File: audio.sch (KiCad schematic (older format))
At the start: 25 parts, among them U6 UDA1334A, U7 LM386, U8 LM386

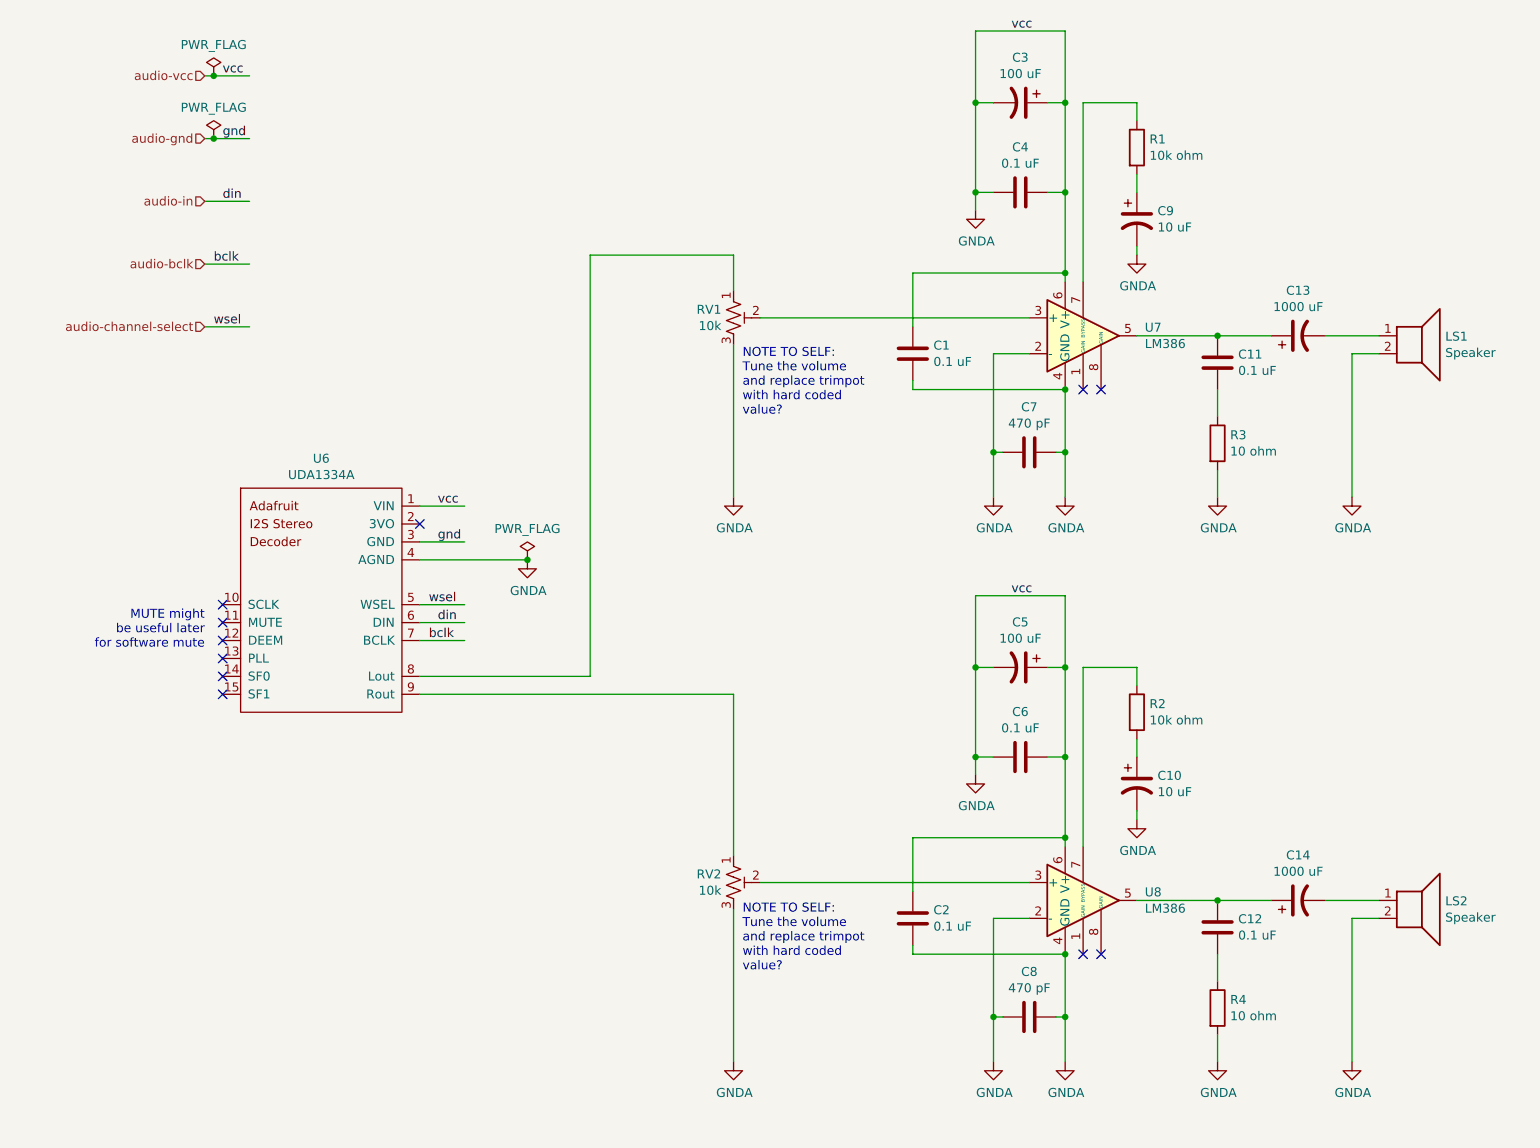
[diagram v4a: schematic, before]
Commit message: Reassign schematic annotation
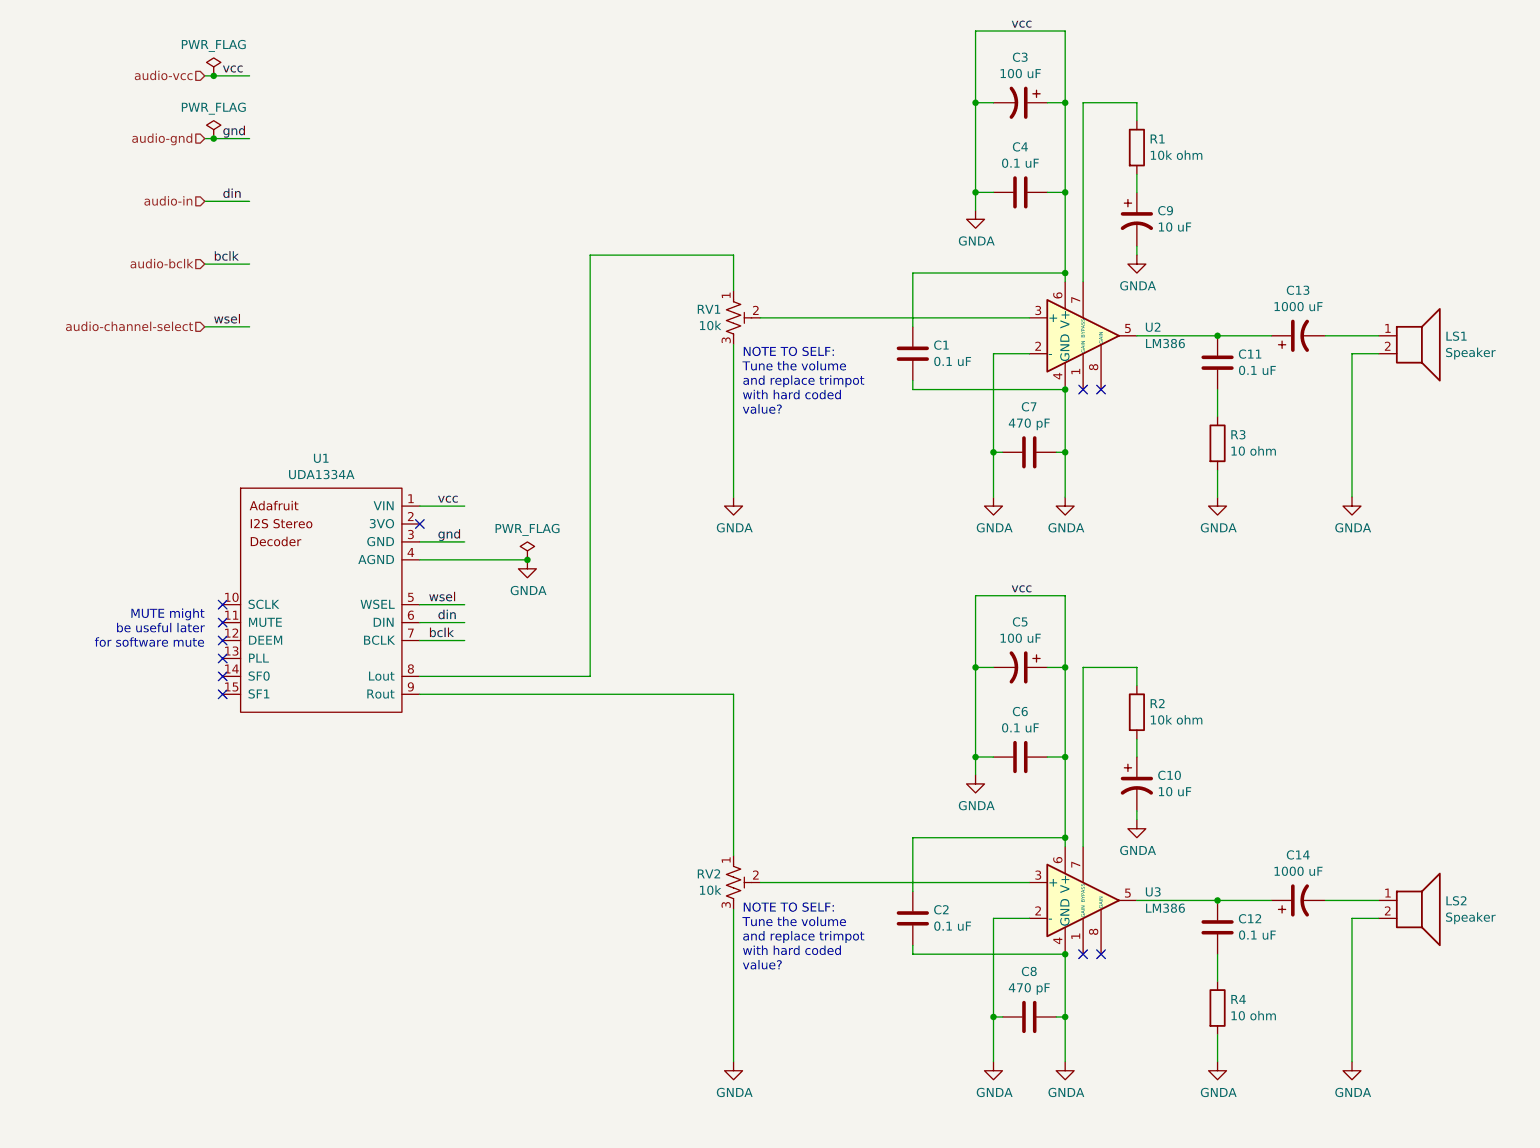
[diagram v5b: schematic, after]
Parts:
- renumbered U6 to U1, U7 to U2, U8 to U3
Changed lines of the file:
@@
 $EndDescr
 $Comp
-L Amplifier_Audio:LM386 U7
+L Amplifier_Audio:LM386 U2
 U 1 1 60687AB3
 P 6600 2350
-F 0 "U7" H 6944 2396 50  0000 L CNN
+F 0 "U2" H 6944 2396 50  0000 L CNN
 F 1 "LM386" H 6944 2305 50  0000 L CNN
 F 2 "" H 6700 2450 50  0001 C CNN
@@
 	4800 2250 6300 2250
 $Comp
-L Amplifier_Audio:LM386 U8
+L Amplifier_Audio:LM386 U3
 U 1 1 606DD65F
 P 6600 5500
-F 0 "U8" H 6944 5546 50  0000 L CNN
+F 0 "U3" H 6944 5546 50  0000 L CNN
 F 1 "LM386" H 6944 5455 50  0000 L CNN
 F 2 "" H 6700 5600 50  0001 C CNN
@@
 	4800 5400 6300 5400
 $Comp
-L adafruit:UDA1334A U6
+L adafruit:UDA1334A U1
 U 1 1 6067F8B5
 P 2350 3850
-F 0 "U6" H 2350 4665 50  0000 C CNN
+F 0 "U1" H 2350 4665 50  0000 C CNN
 F 1 "UDA1334A" H 2350 4574 50  0000 C CNN
 F 2 "" H 2150 4550 50  0001 C CNN
@@
 	2900 3850 3150 3850
 $Comp
-L power:PWR_FLAG #FLG0102
+L power:PWR_FLAG #FLG02
 U 1 1 606CA04F
 P 1750 1250
-F 0 "#FLG0102" H 1750 1325 50  0001 C CNN
+F 0 "#FLG02" H 1750 1325 50  0001 C CNN
 F 1 "PWR_FLAG" H 1750 1423 50  0000 C CNN
 F 2 "" H 1750 1250 50  0001 C CNN
@@
 	1700 900  1750 900
 $Comp
-L power:PWR_FLAG #FLG0101
+L power:PWR_FLAG #FLG01
 U 1 1 6070660E
 P 1750 900
-F 0 "#FLG0101" H 1750 975 50  0001 C CNN
+F 0 "#FLG01" H 1750 975 50  0001 C CNN
 F 1 "PWR_FLAG" H 1750 1073 50  0000 C CNN
 F 2 "" H 1750 900 50  0001 C CNN
@@
 	1750 900  1950 900
 $Comp
-L power:GNDA #PWR0103
+L power:GNDA #PWR08
 U 1 1 6070E011
 P 6100 3250
-F 0 "#PWR0103" H 6100 3000 50  0001 C CNN
+F 0 "#PWR08" H 6100 3000 50  0001 C CNN
 F 1 "GNDA" H 6105 3077 50  0000 C CNN
 F 2 "" H 6100 3250 50  0001 C CNN
@@
 $EndComp
 $Comp
-L power:GNDA #PWR0104
+L power:GNDA #PWR010
 U 1 1 6070E631
 P 6500 3250
-F 0 "#PWR0104" H 6500 3000 50  0001 C CNN
+F 0 "#PWR010" H 6500 3000 50  0001 C CNN
 F 1 "GNDA" H 6505 3077 50  0000 C CNN
 F 2 "" H 6500 3250 50  0001 C CNN
@@
 $EndComp
 $Comp
-L power:GNDA #PWR0105
+L power:GNDA #PWR014
 U 1 1 6070EF51
 P 7350 3250
-F 0 "#PWR0105" H 7350 3000 50  0001 C CNN
+F 0 "#PWR014" H 7350 3000 50  0001 C CNN
 F 1 "GNDA" H 7355 3077 50  0000 C CNN
 F 2 "" H 7350 3250 50  0001 C CNN
@@
 $EndComp
 $Comp
-L power:GNDA #PWR0106
+L power:GNDA #PWR016
 U 1 1 6070F2C0
 P 8100 3250
-F 0 "#PWR0106" H 8100 3000 50  0001 C CNN
+F 0 "#PWR016" H 8100 3000 50  0001 C CNN
 F 1 "GNDA" H 8105 3077 50  0000 C CNN
 F 2 "" H 8100 3250 50  0001 C CNN
@@
 $EndComp
 $Comp
-L power:GNDA #PWR0107
+L power:GNDA #PWR04
 U 1 1 6070F50A
 P 4650 3250
-F 0 "#PWR0107" H 4650 3000 50  0001 C CNN
+F 0 "#PWR04" H 4650 3000 50  0001 C CNN
 F 1 "GNDA" H 4655 3077 50  0000 C CNN
 F 2 "" H 4650 3250 50  0001 C CNN
@@
 $EndComp
 $Comp
-L power:GNDA #PWR0108
+L power:GNDA #PWR09
 U 1 1 60711E7C
 P 6100 6400
-F 0 "#PWR0108" H 6100 6150 50  0001 C CNN
+F 0 "#PWR09" H 6100 6150 50  0001 C CNN
 F 1 "GNDA" H 6105 6227 50  0000 C CNN
 F 2 "" H 6100 6400 50  0001 C CNN
@@
 $EndComp
 $Comp
-L power:GNDA #PWR0109
+L power:GNDA #PWR011
 U 1 1 60711E82
 P 6500 6400
-F 0 "#PWR0109" H 6500 6150 50  0001 C CNN
+F 0 "#PWR011" H 6500 6150 50  0001 C CNN
 F 1 "GNDA" H 6505 6227 50  0000 C CNN
 F 2 "" H 6500 6400 50  0001 C CNN
@@
 $EndComp
 $Comp
-L power:GNDA #PWR0110
+L power:GNDA #PWR015
 U 1 1 60711E88
 P 7350 6400
-F 0 "#PWR0110" H 7350 6150 50  0001 C CNN
+F 0 "#PWR015" H 7350 6150 50  0001 C CNN
 F 1 "GNDA" H 7355 6227 50  0000 C CNN
 F 2 "" H 7350 6400 50  0001 C CNN
@@
 $EndComp
 $Comp
-L power:GNDA #PWR0111
+L power:GNDA #PWR017
 U 1 1 60711E8E
 P 8100 6400
-F 0 "#PWR0111" H 8100 6150 50  0001 C CNN
+F 0 "#PWR017" H 8100 6150 50  0001 C CNN
 F 1 "GNDA" H 8105 6227 50  0000 C CNN
 F 2 "" H 8100 6400 50  0001 C CNN
@@
 $EndComp
 $Comp
-L power:GNDA #PWR0112
+L power:GNDA #PWR05
 U 1 1 60711E94
 P 4650 6400
-F 0 "#PWR0112" H 4650 6150 50  0001 C CNN
+F 0 "#PWR05" H 4650 6150 50  0001 C CNN
 F 1 "GNDA" H 4655 6227 50  0000 C CNN
 F 2 "" H 4650 6400 50  0001 C CNN
@@
 Connection ~ 3500 3600
 $Comp
-L power:PWR_FLAG #FLG0105
+L power:PWR_FLAG #FLG03
 U 1 1 60765574
 P 3500 3600
-F 0 "#FLG0105" H 3500 3675 50  0001 C CNN
+F 0 "#FLG03" H 3500 3675 50  0001 C CNN
 F 1 "PWR_FLAG" H 3500 3773 50  0000 C CNN
 F 2 "" H 3500 3600 50  0001 C CNN
@@
 $EndComp
 $Comp
-L power:GNDA #PWR0113
+L power:GNDA #PWR03
 U 1 1 607206A1
 P 3500 3600
-F 0 "#PWR0113" H 3500 3350 50  0001 C CNN
+F 0 "#PWR03" H 3500 3350 50  0001 C CNN
 F 1 "GNDA" H 3505 3427 50  0000 C CNN
 F 2 "" H 3500 3600 50  0001 C CNN
@@
 	2900 3600 3500 3600
 $Comp
-L power:GNDA #PWR?
+L power:GNDA #PWR012
 U 1 1 60779F44
 P 6900 1900
-F 0 "#PWR?" H 6900 1650 50  0001 C CNN
+F 0 "#PWR012" H 6900 1650 50  0001 C CNN
 F 1 "GNDA" H 6905 1727 50  0000 C CNN
 F 2 "" H 6900 1900 50  0001 C CNN
@@
 $EndComp
 $Comp
-L power:GNDA #PWR?
+L power:GNDA #PWR06
 U 1 1 6077CCCE
 P 6000 1650
-F 0 "#PWR?" H 6000 1400 50  0001 C CNN
+F 0 "#PWR06" H 6000 1400 50  0001 C CNN
 F 1 "GNDA" H 6005 1477 50  0000 C CNN
 F 2 "" H 6000 1650 50  0001 C CNN
@@
 $EndComp
 $Comp
-L power:GNDA #PWR?
+L power:GNDA #PWR013
 U 1 1 60784E23
 P 6900 5050
-F 0 "#PWR?" H 6900 4800 50  0001 C CNN
+F 0 "#PWR013" H 6900 4800 50  0001 C CNN
 F 1 "GNDA" H 6905 4877 50  0000 C CNN
 F 2 "" H 6900 5050 50  0001 C CNN
@@
 $EndComp
 $Comp
-L power:GNDA #PWR?
+L power:GNDA #PWR07
 U 1 1 60787CC6
 P 6000 4800
-F 0 "#PWR?" H 6000 4550 50  0001 C CNN
+F 0 "#PWR07" H 6000 4550 50  0001 C CNN
 F 1 "GNDA" H 6005 4627 50  0000 C CNN
 F 2 "" H 6000 4800 50  0001 C CNN

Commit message: Add ProMicro socket and trimpot footprints.
Create pro micro socket from the kicad-pro-micro footprint and 2 1x12
female header pin vertical footprints. Turns out the kicad-pro-micro
footprint does not have the same measurements as the actual Arduino Pro
Micro I have, so I had to modify it. Will probably use this footprint
without the pin header in the future.

Get Bourns 3362P trimpot from SnapEDA and make some slight
modifications.
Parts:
- C1, C11, C12, C2, C4, C6: footprint (none) -> Capacitor_THT:C_Disc_D5.1mm_W3.2mm_P5.00mm
- C10, C3, C5, C9: footprint (none) -> Capacitor_THT:CP_Radial_D5.0mm_P2.50mm
- C13, C14: footprint (none) -> Capacitor_THT:CP_Radial_D8.0mm_P3.50mm
- C7, C8: footprint (none) -> Capacitor_THT:C_Disc_D4.7mm_W2.5mm_P5.00mm
- R1, R2, R3, R4: footprint (none) -> Resistor_THT:R_Axial_DIN0207_L6.3mm_D2.5mm_P7.62mm_Horizontal
- RV1, RV2: footprint (none) -> 3362P-1-103:TRIM_3362P-1-103
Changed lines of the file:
@@
 F 0 "C4" V 5998 1550 50  0000 C CNN
 F 1 "0.1 uF" V 6089 1550 50  0000 C CNN
-F 2 "" H 6288 1400 50  0001 C CNN
+F 2 "Capacitor_THT:C_Disc_D5.1mm_W3.2mm_P5.00mm" H 6288 1400 50  0001 C CNN
 F 3 "~" H 6250 1550 50  0001 C CNN
 	1    6250 1550
@@
 F 0 "C3" V 5998 1050 50  0000 C CNN
 F 1 "100 uF" V 6089 1050 50  0000 C CNN
-F 2 "" H 6250 1050 50  0001 C CNN
+F 2 "Capacitor_THT:CP_Radial_D5.0mm_P2.50mm" H 6250 1050 50  0001 C CNN
 F 3 "~" H 6250 1050 50  0001 C CNN
 	1    6250 1050
@@
 F 0 "C11" H 7235 2454 50  0000 R CNN
 F 1 "0.1 uF" H 7235 2545 50  0000 R CNN
-F 2 "" H 7388 2350 50  0001 C CNN
+F 2 "Capacitor_THT:C_Disc_D5.1mm_W3.2mm_P5.00mm" H 7388 2350 50  0001 C CNN
 F 3 "~" H 7350 2500 50  0001 C CNN
 	1    7350 2500
@@
 F 0 "R3" H 7420 2996 50  0000 L CNN
 F 1 "10 ohm" H 7420 2905 50  0000 L CNN
-F 2 "" V 7280 2950 50  0001 C CNN
+F 2 "Resistor_THT:R_Axial_DIN0207_L6.3mm_D2.5mm_P7.62mm_Horizontal" V 7280 2950 50  0001 C CNN
 F 3 "~" H 7350 2950 50  0001 C CNN
 	1    7350 2950
@@
 F 0 "C13" V 8052 2350 50  0000 C CNN
 F 1 "1000 uF" V 7961 2350 50  0000 C CNN
-F 2 "" H 7800 2350 50  0001 C CNN
+F 2 "Capacitor_THT:CP_Radial_D8.0mm_P3.50mm" H 7800 2350 50  0001 C CNN
 F 3 "~" H 7800 2350 50  0001 C CNN
 	1    7800 2350
@@
 F 0 "R1" H 6970 1346 50  0000 L CNN
 F 1 "10k ohm" H 6970 1255 50  0000 L CNN
-F 2 "" V 6830 1300 50  0001 C CNN
+F 2 "Resistor_THT:R_Axial_DIN0207_L6.3mm_D2.5mm_P7.62mm_Horizontal" V 6830 1300 50  0001 C CNN
 F 3 "~" H 6900 1300 50  0001 C CNN
 	1    6900 1300
@@
 F 0 "C9" H 7015 1746 50  0000 L CNN
 F 1 "10 uF" H 7015 1655 50  0000 L CNN
-F 2 "" H 6900 1700 50  0001 C CNN
+F 2 "Capacitor_THT:CP_Radial_D5.0mm_P2.50mm" H 6900 1700 50  0001 C CNN
 F 3 "~" H 6900 1700 50  0001 C CNN
 	1    6900 1700
@@
 F 0 "C7" V 6552 3000 50  0000 C CNN
 F 1 "470 pF" V 6461 3000 50  0000 C CNN
-F 2 "" H 6338 2850 50  0001 C CNN
+F 2 "Capacitor_THT:C_Disc_D4.7mm_W2.5mm_P5.00mm" H 6338 2850 50  0001 C CNN
 F 3 "~" H 6300 3000 50  0001 C CNN
 	1    6300 3000
@@
 F 0 "C1" H 5765 2496 50  0000 L CNN
 F 1 "0.1 uF" H 5765 2405 50  0000 L CNN
-F 2 "" H 5688 2300 50  0001 C CNN
+F 2 "Capacitor_THT:C_Disc_D5.1mm_W3.2mm_P5.00mm" H 5688 2300 50  0001 C CNN
 F 3 "~" H 5650 2450 50  0001 C CNN
 	1    5650 2450
@@
 F 0 "RV1" H 4582 2296 50  0000 R CNN
 F 1 "10k" H 4582 2205 50  0000 R CNN
-F 2 "" H 4650 2250 50  0001 C CNN
+F 2 "3362P-1-103:TRIM_3362P-1-103" H 4650 2250 50  0001 C CNN
 F 3 "~" H 4650 2250 50  0001 C CNN
 	1    4650 2250
@@
 F 0 "C6" V 5998 4700 50  0000 C CNN
 F 1 "0.1 uF" V 6089 4700 50  0000 C CNN
-F 2 "" H 6288 4550 50  0001 C CNN
+F 2 "Capacitor_THT:C_Disc_D5.1mm_W3.2mm_P5.00mm" H 6288 4550 50  0001 C CNN
 F 3 "~" H 6250 4700 50  0001 C CNN
 	1    6250 4700
@@
 F 0 "C5" V 5998 4200 50  0000 C CNN
 F 1 "100 uF" V 6089 4200 50  0000 C CNN
-F 2 "" H 6250 4200 50  0001 C CNN
+F 2 "Capacitor_THT:CP_Radial_D5.0mm_P2.50mm" H 6250 4200 50  0001 C CNN
 F 3 "~" H 6250 4200 50  0001 C CNN
 	1    6250 4200
@@
 F 0 "C12" H 7235 5604 50  0000 R CNN
 F 1 "0.1 uF" H 7235 5695 50  0000 R CNN
-F 2 "" H 7388 5500 50  0001 C CNN
+F 2 "Capacitor_THT:C_Disc_D5.1mm_W3.2mm_P5.00mm" H 7388 5500 50  0001 C CNN
 F 3 "~" H 7350 5650 50  0001 C CNN
 	1    7350 5650
@@
 F 0 "R4" H 7420 6146 50  0000 L CNN
 F 1 "10 ohm" H 7420 6055 50  0000 L CNN
-F 2 "" V 7280 6100 50  0001 C CNN
+F 2 "Resistor_THT:R_Axial_DIN0207_L6.3mm_D2.5mm_P7.62mm_Horizontal" V 7280 6100 50  0001 C CNN
 F 3 "~" H 7350 6100 50  0001 C CNN
 	1    7350 6100
@@
 F 0 "C14" V 8052 5500 50  0000 C CNN
 F 1 "1000 uF" V 7961 5500 50  0000 C CNN
-F 2 "" H 7800 5500 50  0001 C CNN
+F 2 "Capacitor_THT:CP_Radial_D8.0mm_P3.50mm" H 7800 5500 50  0001 C CNN
 F 3 "~" H 7800 5500 50  0001 C CNN
 	1    7800 5500
@@
 F 0 "R2" H 6970 4496 50  0000 L CNN
 F 1 "10k ohm" H 6970 4405 50  0000 L CNN
-F 2 "" V 6830 4450 50  0001 C CNN
+F 2 "Resistor_THT:R_Axial_DIN0207_L6.3mm_D2.5mm_P7.62mm_Horizontal" V 6830 4450 50  0001 C CNN
 F 3 "~" H 6900 4450 50  0001 C CNN
 	1    6900 4450
@@
 F 0 "C10" H 7015 4896 50  0000 L CNN
 F 1 "10 uF" H 7015 4805 50  0000 L CNN
-F 2 "" H 6900 4850 50  0001 C CNN
+F 2 "Capacitor_THT:CP_Radial_D5.0mm_P2.50mm" H 6900 4850 50  0001 C CNN
 F 3 "~" H 6900 4850 50  0001 C CNN
 	1    6900 4850
@@
 F 0 "C8" V 6552 6150 50  0000 C CNN
 F 1 "470 pF" V 6461 6150 50  0000 C CNN
-F 2 "" H 6338 6000 50  0001 C CNN
+F 2 "Capacitor_THT:C_Disc_D4.7mm_W2.5mm_P5.00mm" H 6338 6000 50  0001 C CNN
 F 3 "~" H 6300 6150 50  0001 C CNN
 	1    6300 6150
@@
 F 0 "C2" H 5765 5646 50  0000 L CNN
 F 1 "0.1 uF" H 5765 5555 50  0000 L CNN
-F 2 "" H 5688 5450 50  0001 C CNN
+F 2 "Capacitor_THT:C_Disc_D5.1mm_W3.2mm_P5.00mm" H 5688 5450 50  0001 C CNN
 F 3 "~" H 5650 5600 50  0001 C CNN
 	1    5650 5600
@@
 F 0 "RV2" H 4582 5446 50  0000 R CNN
 F 1 "10k" H 4582 5355 50  0000 R CNN
-F 2 "" H 4650 5400 50  0001 C CNN
+F 2 "3362P-1-103:TRIM_3362P-1-103" H 4650 5400 50  0001 C CNN
 F 3 "~" H 4650 5400 50  0001 C CNN
 	1    4650 5400
